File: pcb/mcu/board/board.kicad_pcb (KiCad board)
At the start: 2 copper layers, 14 parts, among them J1 Conn_02x04_Odd_Even, J2 Conn_01x01_Female, J3 Conn_01x01_Female, J4 Conn_01x01_Female, J5 Conn_01x01_Female, J6 Conn_01x01_Female, J7 Conn_01x01_Female, Y1 Crystal

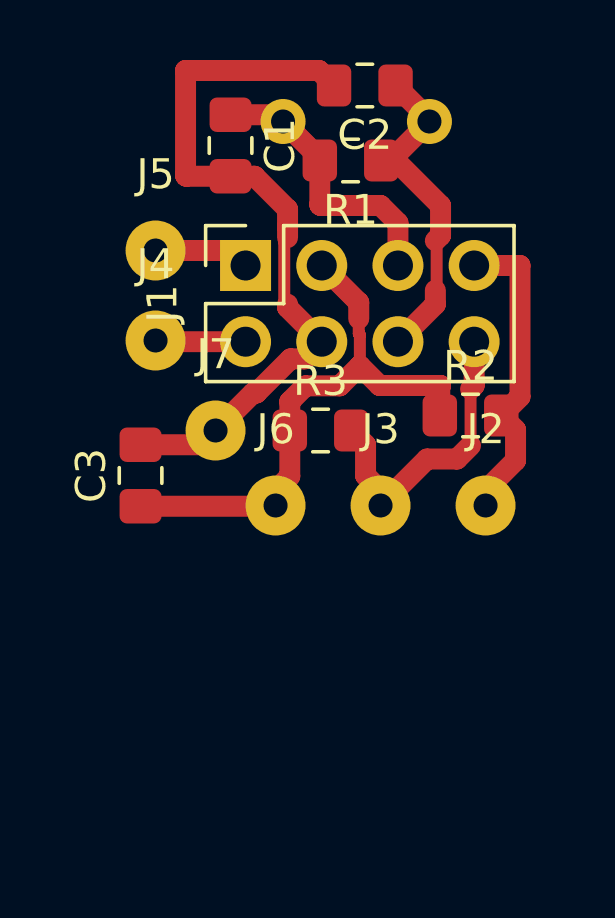
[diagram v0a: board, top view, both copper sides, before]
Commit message: Ddded additional provision.
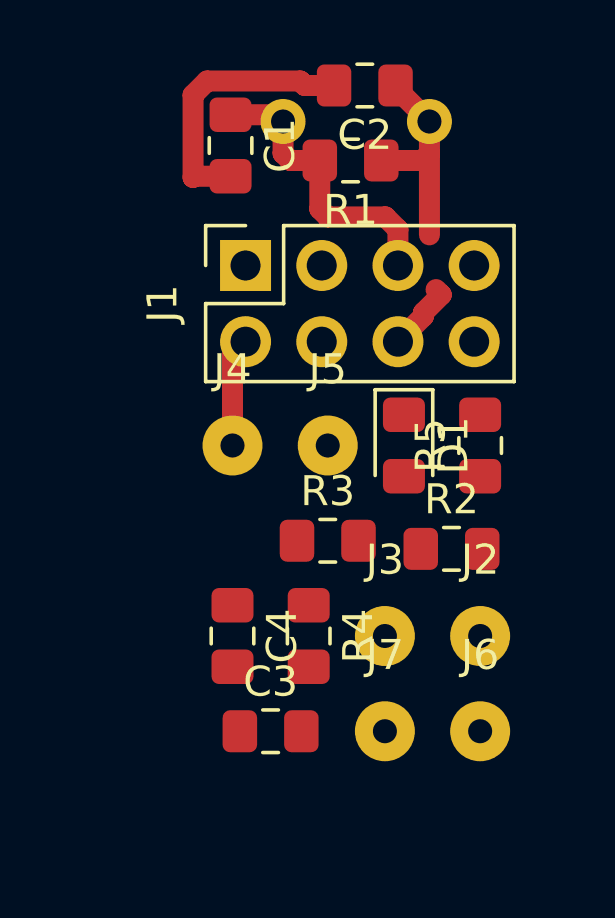
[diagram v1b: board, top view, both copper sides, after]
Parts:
- added C4: 100n, Capacitor_SMD:C_0805_2012Metric_Pad1.15x1.40mm_HandSolder, F.Cu at (75.6, 69.8)
- added D1: LED, LED_SMD:LED_0805_2012Metric_Pad1.15x1.40mm_HandSolder, F.Cu at (81.3, 63.5)
- added R4: 1K, Resistor_SMD:R_0805_2012Metric_Pad1.15x1.40mm_HandSolder, F.Cu at (78.1, 69.8)
- added R5: 1K, Resistor_SMD:R_0805_2012Metric_Pad1.15x1.40mm_HandSolder, F.Cu at (83.8, 63.5)
- moved J7 11.5 mm to (80.6, 73.0)
- moved J6 10.2 mm to (83.8, 73.0)
- moved C3 9.56 mm to (76.8, 73.0), turned to 0 degrees
- moved J5 8.67 mm to (78.7, 63.5)
- moved R2 4.49 mm to (82.9, 66.9)
- moved J2 4.35 mm to (83.8, 69.8)
- moved J3 4.35 mm to (80.6, 69.8)
- moved J4 4.34 mm to (75.6, 63.5)
- moved R3 3.68 mm to (78.7, 66.7)
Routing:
- net VCC: track 18.8 -> 0.00 mm
- net GND: track 25.7 -> 8.97 mm
- net SCL: track 10.4 -> 0.00 mm
- net SDA: track 10.3 -> 0.00 mm
- net PG4: track 3.21 -> 0.00 mm
- net XTAL1: track 11.6 -> 9.56 mm
- net ~RST: track 3.02 -> 3.64 mm
- net XTAL2: track 9.40 -> 9.93 mm

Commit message: Added DTR with a capacitor.
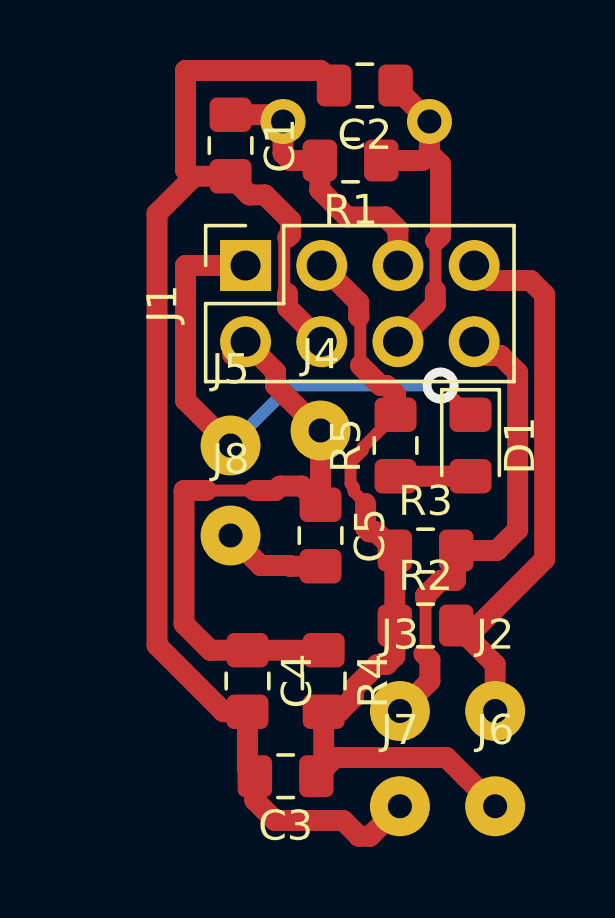
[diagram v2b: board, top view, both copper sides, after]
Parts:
- added C5: 100n, Capacitor_SMD:C_0805_2012Metric_Pad1.15x1.40mm_HandSolder, F.Cu at (78.5, 66.5)
- added J8: DTR, Connector_Wire:SolderWirePad_1x01_Drill0.8mm, F.Cu at (75.5, 66.5)
- J2: value Conn_01x01_Female -> SCL
- J3: value Conn_01x01_Female -> SDA
- J4: value Conn_01x01_Female -> ~RST
- J5: value Conn_01x01_Female -> PG4
- J6: value Conn_01x01_Female -> VCC
- J7: value Conn_01x01_Female -> GND
- moved R3 3.28 mm to (82.0, 67.0)
- moved J5 3.24 mm to (75.5, 63.5)
- moved J4 2.98 mm to (78.5, 63.0)
- moved R5 2.82 mm to (81.0, 63.5)
- moved R2 2.70 mm to (82.0, 69.5)
- moved J2 2.55 mm to (84.3, 72.3)
- moved J3 2.55 mm to (81.1, 72.3)
- moved J6 2.55 mm to (84.3, 75.5)
- moved J7 2.55 mm to (81.1, 75.5)
- moved D1 2.22 mm to (83.5, 63.5)
- moved C3 1.58 mm to (77.3, 74.5), turned to 180 degrees
- moved C4 1.58 mm to (76.1, 71.3)
- moved R4 1.58 mm to (78.6, 71.3)
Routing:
- net GND: track 8.97 -> 46.3 mm
- net VCC: track 0.00 -> 28.0 mm
- net SCL: track 0.00 -> 18.8 mm
- net ~RST: track 3.64 -> 21.6 mm
- net PG4: track 0.00 -> 17.9 mm, vias 0 -> 1
- net SDA: track 0.00 -> 16.2 mm
- net Net-(C5-Pad2): track 0.00 -> 3.42 mm
- net Net-(D1-Pad2): track 0.00 -> 2.50 mm
- net XTAL1: track 9.56 -> 11.5 mm

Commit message: New kicad tested.
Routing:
- net GND: track 46.3 -> 47.2 mm
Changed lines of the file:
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@@
-(kicad_pcb (version 20171130) (host pcbnew 5.1.1)
+(kicad_pcb (version 20171130) (host pcbnew 5.1.2)
   (general
     (thickness 1.6)
@@
   )
   (setup
-    (last_trace_width 0.7)
+    (last_trace_width 0.4)
     (user_trace_width 0.4)
     (user_trace_width 0.5)
@@
   (segment (start 76.065 74.28) (end 76.31 74.525) (width 0.7) (layer F.Cu) (net 1))
   (segment (start 76.065 72.375) (end 76.065 74.28) (width 0.7) (layer F.Cu) (net 1))
-  (segment (start 80.145511 76.524489) (end 81.145 75.525) (width 0.7) (layer F.Cu) (net 1))
-  (segment (start 79.780997 76.524489) (end 80.145511 76.524489) (width 0.7) (layer F.Cu) (net 1))
-  (segment (start 79.256508 76) (end 79.780997 76.524489) (width 0.7) (layer F.Cu) (net 1))
-  (segment (start 76.985 76) (end 79.256508 76) (width 0.7) (layer F.Cu) (net 1))
-  (segment (start 76.31 75.325) (end 76.985 76) (width 0.7) (layer F.Cu) (net 1))
-  (segment (start 76.31 74.525) (end 76.31 75.325) (width 0.7) (layer F.Cu) (net 1))
   (segment (start 77.289999 56.677999) (end 77.289999 58.322001) (width 0.4) (layer F.Cu) (net 1))
   (segment (start 77.289999 58.322001) (end 77.400001 58.432003) (width 0.4) (layer F.Cu) (net 1))
   (segment (start 77.5 56.467998) (end 77.289999 56.677999) (width 0.4) (layer F.Cu) (net 1))
-  (segment (start 76.065 72.375) (end 75.265 72.375) (width 0.7) (layer F.Cu) (net 1))
-  (segment (start 73.050498 55.764482) (end 74.24999 54.56499) (width 0.7) (layer F.Cu) (net 1))
-  (segment (start 73.050498 70.160498) (end 73.050498 55.764482) (width 0.7) (layer F.Cu) (net 1))
-  (segment (start 75.265 72.375) (end 73.050498 70.160498) (width 0.7) (layer F.Cu) (net 1))
   (segment (start 74 54.315) (end 74.24999 54.56499) (width 0.7) (layer F.Cu) (net 1))
   (segment (start 74 51) (end 74 54.315) (width 0.7) (layer F.Cu) (net 1))
@@
   (segment (start 75.5 54.525) (end 76.123372 55.148372) (width 0.7) (layer F.Cu) (net 1))
   (segment (start 76.123372 55.148372) (end 76.648372 55.148372) (width 0.7) (layer F.Cu) (net 1))
+  (segment (start 80.145511 76.524489) (end 81.145 75.525) (width 0.7) (layer F.Cu) (net 1))
+  (segment (start 76.31 74.525) (end 76.31 75.89) (width 0.7) (layer F.Cu) (net 1))
+  (segment (start 79.780997 76.524489) (end 80.145511 76.524489) (width 0.7) (layer F.Cu) (net 1))
+  (segment (start 76.31 75.89) (end 76.3 75.9) (width 0.7) (layer F.Cu) (net 1))
+  (segment (start 76.3 75.9) (end 76.4 76) (width 0.7) (layer F.Cu) (net 1))
+  (segment (start 76.4 76) (end 79.256508 76) (width 0.7) (layer F.Cu) (net 1))
+  (segment (start 79.256508 76) (end 79.780997 76.524489) (width 0.7) (layer F.Cu) (net 1))
+  (segment (start 73.050498 55.764482) (end 74.24999 54.56499) (width 0.7) (layer F.Cu) (net 1))
+  (segment (start 73.050498 71.050498) (end 73.050498 55.764482) (width 0.7) (layer F.Cu) (net 1))
+  (segment (start 76.065 72.375) (end 74.375 72.375) (width 0.7) (layer F.Cu) (net 1))
+  (segment (start 74.375 72.375) (end 73.050498 71.050498) (width 0.7) (layer F.Cu) (net 1))
   (segment (start 77.025 52.475) (end 77.25 52.7) (width 0.7) (layer F.Cu) (net 2))
   (segment (start 75.5 52.475) (end 77.025 52.475) (width 0.7) (layer F.Cu) (net 2))
@@
   (segment (start 80.975 67) (end 80.351628 66.376628) (width 0.7) (layer F.Cu) (net 6))
   (segment (start 80.123372 66.376628) (end 80 66.253256) (width 0.7) (layer F.Cu) (net 6))
-  (segment (start 80 66.253256) (end 80 65.431388) (width 0.7) (layer F.Cu) (net 6))
-  (segment (start 80.376628 63.098372) (end 81 62.475) (width 0.4) (layer F.Cu) (net 6))
-  (segment (start 79.899491 63.575509) (end 80.376628 63.098372) (width 0.4) (layer F.Cu) (net 6))
-  (segment (start 79.60001 65.031398) (end 79.60001 64.880754) (width 0.4) (layer F.Cu) (net 6))
-  (segment (start 80 65.431388) (end 79.60001 65.031398) (width 0.4) (layer F.Cu) (net 6))
-  (segment (start 79.5 64.071248) (end 79.899491 63.671757) (width 0.4) (layer F.Cu) (net 6))
-  (segment (start 79.5 64.780744) (end 79.5 64.071248) (width 0.4) (layer F.Cu) (net 6))
-  (segment (start 79.60001 64.880754) (end 79.5 64.780744) (width 0.4) (layer F.Cu) (net 6))
-  (segment (start 79.899491 63.671757) (end 79.899491 63.575509) (width 0.4) (layer F.Cu) (net 6))
   (segment (start 79.77 59.197998) (end 79.786001 59.213999) (width 0.7) (layer F.Cu) (net 6))
   (segment (start 78.54 57.5) (end 79.77 58.73) (width 0.7) (layer F.Cu) (net 6))
@@
   (segment (start 81 62.475) (end 81 61.8) (width 0.7) (layer F.Cu) (net 6))
   (segment (start 81 61.8) (end 80.7 61.5) (width 0.7) (layer F.Cu) (net 6))
+  (segment (start 80 65.431388) (end 80 66.253256) (width 0.4) (layer F.Cu) (net 6))
+  (segment (start 79.60001 65.031398) (end 80 65.431388) (width 0.4) (layer F.Cu) (net 6))
+  (segment (start 79.5 64.780744) (end 79.60001 64.880754) (width 0.4) (layer F.Cu) (net 6))
+  (segment (start 81 62.475) (end 79.899491 63.575509) (width 0.4) (layer F.Cu) (net 6))
+  (segment (start 79.899491 63.671757) (end 79.5 64.071248) (width 0.4) (layer F.Cu) (net 6))
+  (segment (start 79.5 64.071248) (end 79.5 64.780744) (width 0.4) (layer F.Cu) (net 6))
+  (segment (start 79.899491 63.575509) (end 79.899491 63.671757) (width 0.4) (layer F.Cu) (net 6))
+  (segment (start 79.60001 64.880754) (end 79.60001 65.031398) (width 0.4) (layer F.Cu) (net 6))
   (segment (start 75.565 60.475) (end 76 60.04) (width 0.7) (layer F.Cu) (net 7))
   (segment (start 76 60.04) (end 77 61.04) (width 0.7) (layer F.Cu) (net 7))
@@
   (segment (start 82.5 61.5) (end 77.5 61.5) (width 0.4) (layer B.Cu) (net 8))
   (segment (start 77.5 61.5) (end 75.5 63.5) (width 0.4) (layer B.Cu) (net 8))
-  (segment (start 83.475 62.475) (end 82.5 61.5) (width 0.4) (layer F.Cu) (net 8))
-  (segment (start 83.5 62.475) (end 83.475 62.475) (width 0.4) (layer F.Cu) (net 8))
   (via (at 82.5 61.5) (size 1.2) (drill 0.6) (layers F.Cu B.Cu) (net 8))
   (segment (start 74 62) (end 75.5 63.5) (width 0.7) (layer F.Cu) (net 8))
   (segment (start 76 57.5) (end 74 57.5) (width 0.7) (layer F.Cu) (net 8))
   (segment (start 74 57.5) (end 74 62) (width 0.7) (layer F.Cu) (net 8))
+  (segment (start 83.475 62.475) (end 82.5 61.5) (width 0.7) (layer F.Cu) (net 8))
+  (segment (start 83.5 62.475) (end 83.475 62.475) (width 0.7) (layer F.Cu) (net 8))
   (segment (start 81 64.525) (end 83.5 64.525) (width 0.7) (layer F.Cu) (net 9))
   (segment (start 77.475 67.525) (end 78.5 67.525) (width 0.7) (layer F.Cu) (net 10))
